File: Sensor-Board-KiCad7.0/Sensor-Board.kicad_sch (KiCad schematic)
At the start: 78 parts, among them J1 110990030, J11 9401-0-15-15-23-27-10-0, J2 9401-0-15-15-23-27-10-0, J3 9401-0-15-15-23-27-10-0, J4 9401-0-15-15-23-27-10-0, J5 9401-0-15-15-23-27-10-0, J6 9401-0-15-15-23-27-10-0, J7 9401-0-15-15-23-27-10-0, J8 9401-0-15-15-23-27-10-0, J9 9401-0-15-15-23-27-10-0, U1 LMV721, U10 BME680, U11 NAU7802_24-bit_ADC, U12 NAU7802_24-bit_ADC, U13 TCA9548AMRGER, U2 LMV721, U20 MMBFJ177LT1G, U27 MMBFJ177LT1G, U28 MMBFJ177LT1G, U3 LMV721, U4 LMV721, U5 LMV721, U6 OPAMP, U7 PS1-NO2-50, U8 PS1-CO-1000, U9 PS1-SO2-50

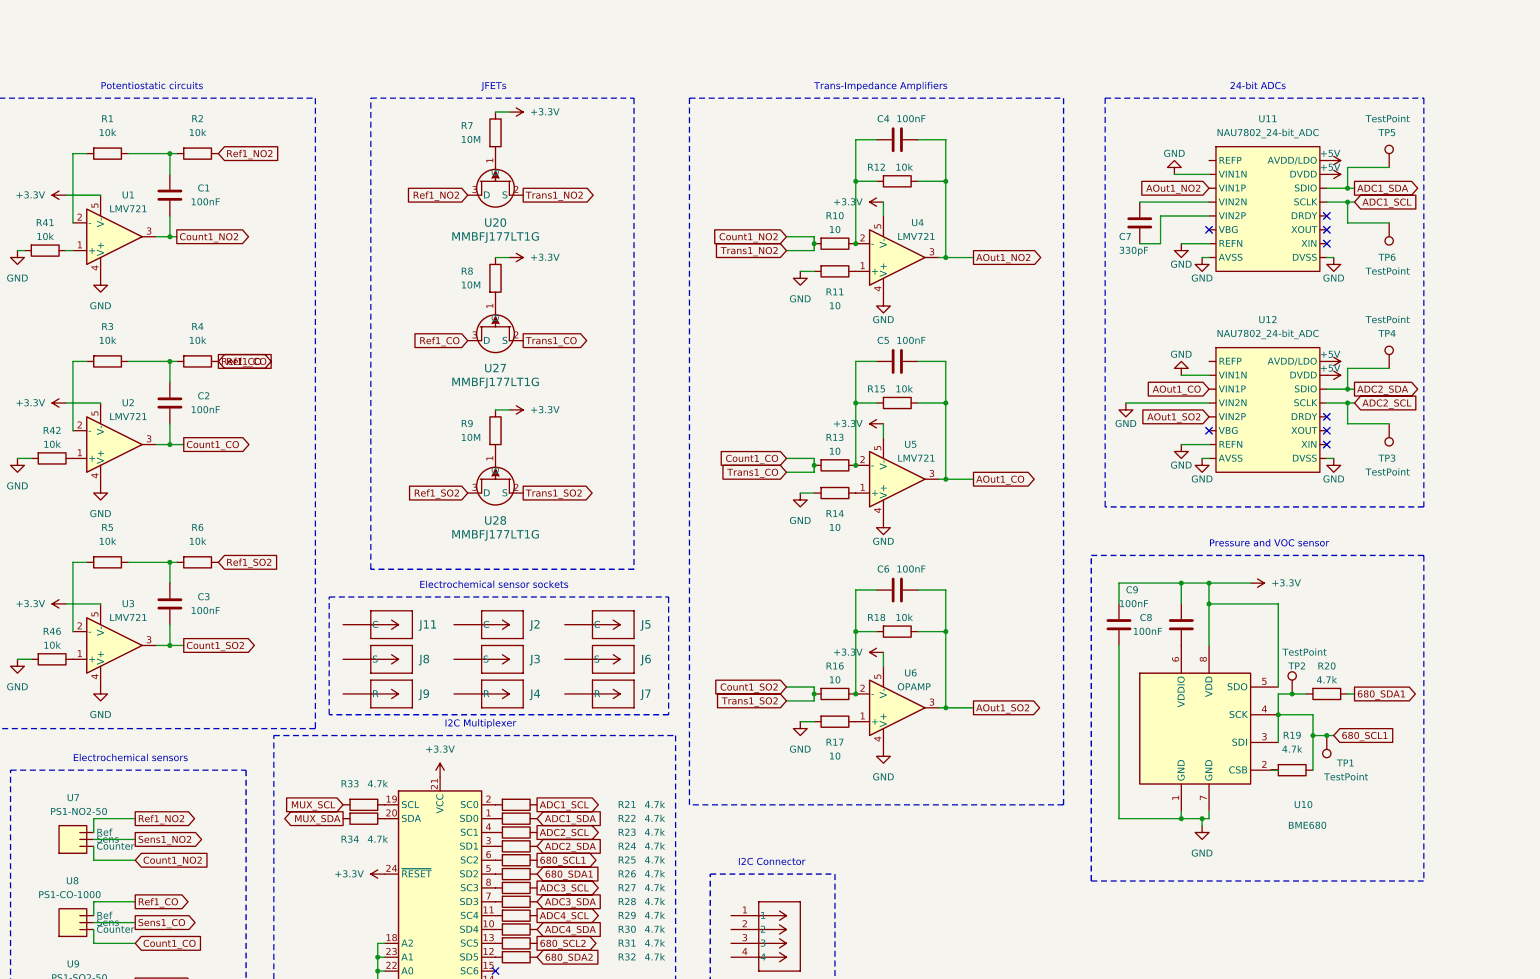
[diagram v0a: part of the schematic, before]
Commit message: Final check
Added 10k resistors to + input of opamps. Added JFET symbol and footprint. Changed opamp from LMV721 to OPA386 to conform to 3-electrode design sheet. Fixed circuit for BME680. Added test points.
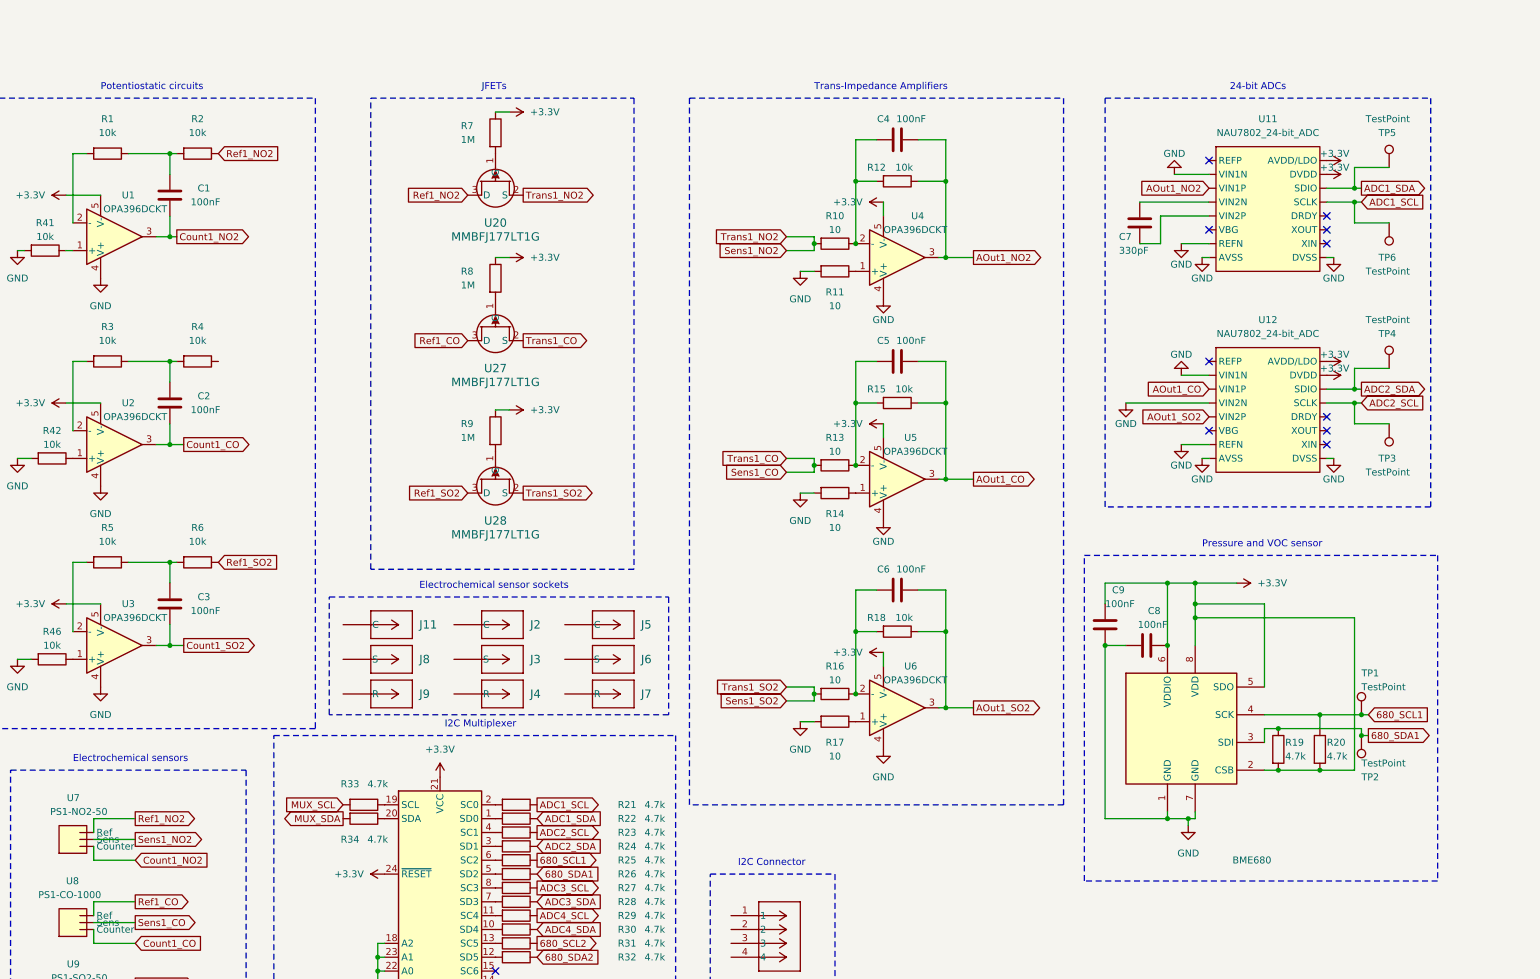
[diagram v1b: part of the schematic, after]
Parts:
- R7, R8, R9: value 10M -> 1M
- U1, U2, U3, U4, U5: value LMV721 -> OPA396DCKT
- U6: value OPAMP -> OPA396DCKT
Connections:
- net +5V is gone; now on net GND: U11. (XOUT), U12. (XOUT)
- net +3.3V: now also C8.2, R19.2, R20.2, U10.2 (CSB), U10.6 (VDDIO), U11. (XOUT), U12. (XOUT); no longer C8.1
- net 680_SCL1: now also R20.1; no longer R19.1, R20.2, TP2.1, U10.3 (SDI)
- net 680_SDA1: now also R19.1, TP2.1, U10.3 (SDI); no longer R20.1
- net Count1_CO: no longer R13.2, U27.2 (S)
- net Count1_NO2: no longer R10.2, U20.2 (S)
- net Count1_SO2: no longer R16.2, U28.2 (S)
- net GND: now also C8.1
- net Ref1_CO: no longer R4.1
- net Sens1_CO: now also R13.2, U27.2 (S)
- net Sens1_NO2: now also R10.2, U20.2 (S)
- net Sens1_SO2: now also R16.2, U28.2 (S)
- no-connect marks 12 -> 14
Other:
- moved on the sheet: C8, C9

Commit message: Updated symbols + footprints
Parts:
- removed C5, C6: 100nF, symbol Device:C
- removed C7: 330pF, symbol Device:C
- removed R10, R11, R13, R14, R16, R17: 10, symbol Device:R
- removed R12, R15, R18: 10k, symbol Device:R
- removed TP3, TP4, TP5, TP6: TestPoint, symbol Connector:TestPoint
- removed U1, U2, U3, U4, U5, U6: OPA396DCKT, symbol pspice:OPAMP
- removed U11, U12: NAU7802_24-bit_ADC, symbol ADCs:NAU7802_24-bit_ADC
- removed U20, U27, U28: MMBFJ177LT1G, SOT_77LT1G_ONS, symbol MMBFJ177LT1-D:MMBFJ177LT1G
- removed U7: PS1-NO2-50, symbol ElectrochemcialSensors:PS1-NO2-50
- removed U8: PS1-CO-1000, symbol ElectrochemcialSensors:PS1-CO-1000
- removed U9: PS1-SO2-50, symbol ElectrochemcialSensors:PS1-SO2-50
- added C19, C20, C21: 100nF, symbol Device:C
- added R52, R53, R67, R68: 10, symbol Device:R
- added R54, R56, R57, R69: 10k, symbol Device:R
- added R55: 100k, symbol Device:R
- added TP11, TP12, TP13, TP14, TP15, TP16, TP17, TP18: TestPoint, symbol Connector:TestPoint
- added U1, U2, U27, U28, U3, U34: OPA396DCKT, SC_96DCKT_TEX, symbol OPA396DCKT:OPA396DCKT
- added U20, U32, U33: MMBFJ177LT1, SOT-23-3_1P4X3P040_ONS, symbol MMBFJ177LT1G:MMBFJ177LT1
- added U4, U5: NAU7802SGI, SOI16_NAU7802SGI_NUV, symbol NAU7802:NAU7802SGI
- C4: value 100nF -> 330pF
- R1, R4: value 10k -> 100k
- R41, R42, R46: value 10k -> 1M
- R7, R8: value 1M -> 10
- R9: value 1M -> 10k
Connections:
- net 680_SDA1 is gone; now on net 680_SCL1: R19.1, R26.1, TP2.1, U10.3 (SDI)
- net +3.3V: now also J1.4, R41.2, R42.2, R46.2, U1.2 (V-), U2.2 (V-), U27.2 (V-), U28.2 (V-), U3.2 (V-), U34.2 (V-), U4.15 (DVDD), U5.15 (DVDD); no longer R7.1, R8.1, R9.1
- net ADC1_SCL: now also TP15.1, U4.13 (SCLK)
- net ADC1_SDA: now also TP14.1, U4.14 (SDIO)
- net ADC2_SCL: now also TP18.1, U5.13 (SCLK)
- net ADC2_SDA: now also TP17.1, U5.14 (SDIO)
- net AOut1_CO: now also C19.1, R54.1, U28.4 (OUT), U5.3 (VIN1P)
- net AOut1_NO2: now also C3.1, R9.1, U27.4 (OUT), U4.3 (VIN1P); no longer C4.1
- net AOut1_SO2: now also C21.1, R69.1, U34.4 (OUT), U5.5 (VIN2P)
- net Count1_CO: now also C1.2, J2. (C), U2.4 (OUT); no longer C2.2
- net Count1_NO2: now also J11. (C), C20.2, U1.4 (OUT); no longer C1.2
- net Count1_SO2: now also C2.2, J5. (C), U3.4 (OUT); no longer C3.2
- net GND: now also J1.1, R1.2, R4.2, R7.2, R53.2, R55.2, R68.2, U1.5 (V+), U2.5 (V+), U27.5 (V+), U28.5 (V+), U3.5 (V+), U34.5 (V+), U4.2 (VIN1N), U4.7 (REFN), U4.8 (AVSS), U4.9 (DVSS), U5.2 (VIN1N), U5.4 (VIN2N), U5.7 (REFN), U5.8 (AVSS), U5.9 (DVSS); no longer R41.2, R42.2, R46.2
- net MUX_SCL: now also J1.3, TP11.1
- net MUX_SDA: now also J1.2, TP12.1
- net Ref1_CO: now also J4. (R), R3.1, U32.1 (D)
- net Ref1_NO2: now also J9. (R), R57.1, U20.1 (D); no longer R2.1
- net Ref1_SO2: now also J7. (R), U33.1 (D)
- net Sens1_CO: now also J3. (S), R52.2, U32.2 (S)
- net Sens1_NO2: now also J8. (S), R8.2, U20.2 (S)
- net Sens1_SO2: now also J6. (S), R67.2, U33.2 (S)
- net at R9.2: now also C3.2, R8.1, U27.3 (-IN)
- net at R42.1: now also U32.3 (G)
- net at R3.2: now also C1.1, R2.1
- net at R46.1: now also U33.3 (G)
- net at R5.2: now also U3.3 (-IN)
- net at R5.1, R6.2: now also C2.1; no longer C3.1
- net at R41.1: now also U20.3 (G)
- net at C4.2: now also U4.5 (VIN2P)
- net at R4.1: now also U3.1 (+IN)
- new net: C19.2, R52.1, R54.2, U28.3 (-IN)
- new net: TP16.1, U5.16 (AVDD/LDO)
- new net: C4.1, U4.4 (VIN2N)
- new net: R7.1, U27.1 (+IN)
- new net: R53.1, U28.1 (+IN)
- new net: TP13.1, U4.16 (AVDD/LDO)
- new net: R2.2, U2.3 (-IN)
- new net: C20.1, R56.1, R57.2
- new net: C21.2, R67.1, R69.2, U34.3 (-IN)
- new net: R68.1, U34.1 (+IN)
- new net: R1.1, U2.1 (+IN)
- new net: R56.2, U1.3 (-IN)
- new net: R55.1, U1.1 (+IN)
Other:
- note removed: "Electrochemical sensors"
- moved on the sheet: C8, C9, J1, J11, J8, J9, R19, R20, R21, R22, R23, R24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

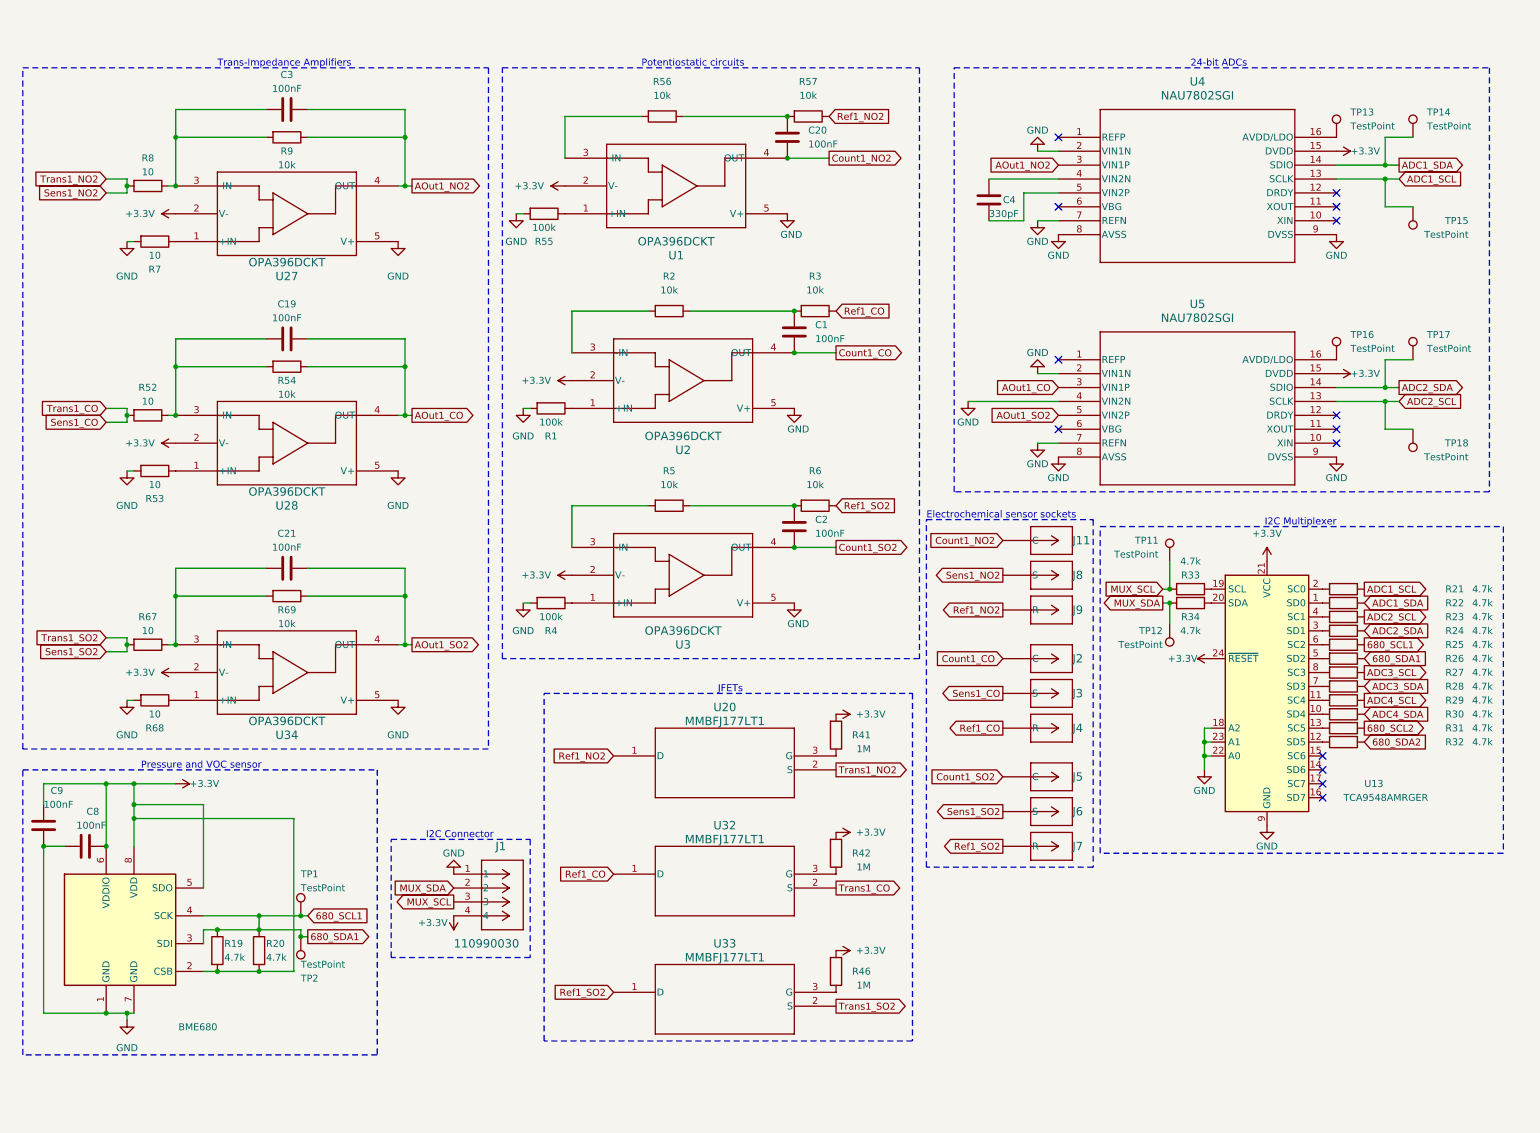
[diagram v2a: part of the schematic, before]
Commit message: Fixed a bunch of errors
Updated OPA396 symbol + footprints
Updated NAU7802 symbol + footprints
Updated MMBFJ177LT1 symbol + footprints
Updated EChem socket symbol + footprints
Updated I2C connector symbol + footprints
Fixed connection issues with EChem sockets
Removed net labels from EChem sockets
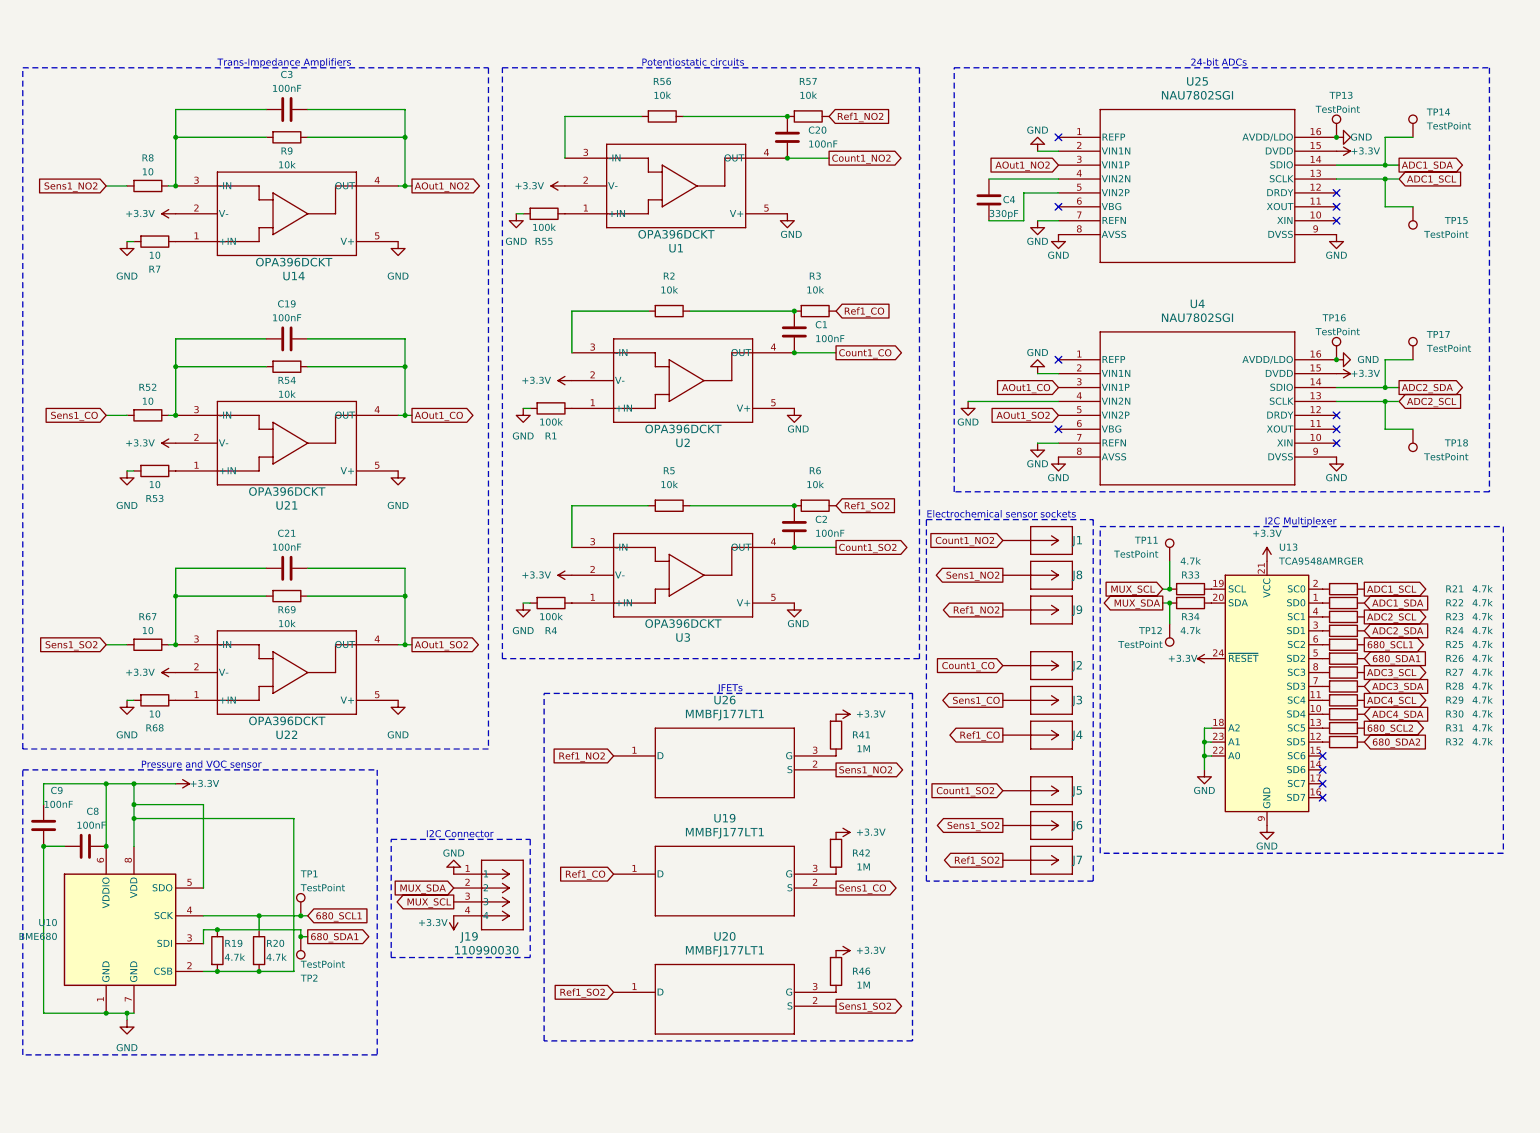
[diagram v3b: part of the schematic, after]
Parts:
- removed J1: 110990030, CONN_110990030_SEE, symbol 110990030:110990030
- removed J11, J2, J3, J4, J5, J6, J7, J8, J9: 9401-0-15-15-23-27-10-0, CONN_0384-0-67-80-23-27-10-0_MIM, symbol EChem Socket:9401-0-15-15-23-27-10-0
- removed U27, U28, U34: OPA396DCKT, SC_96DCKT_TEX, symbol OPA396DCKT:OPA396DCKT
- removed U32, U33: MMBFJ177LT1, SOT-23-3_1P4X3P040_ONS, symbol MMBFJ177LT1G:MMBFJ177LT1
- removed U5: NAU7802SGI, SOI16_NAU7802SGI_NUV, symbol NAU7802:NAU7802SGI
- added J1, J2, J3, J4, J5, J6, J7, J8, J9: 9401-0-15-15-23-27-10-0, CONN_0384-0-67-80-23-27-10-0_MIM, symbol EChem socket:9401-0-15-15-23-27-10-0
- added J19: 110990030, CONN_110990030_SEE, symbol I2C Connector:110990030
- added U14, U21, U22: OPA396DCKT, SC_96DCKT_TEX, symbol OPA396DCKT:OPA396DCKT
- added U19, U26: MMBFJ177LT1, SOT-23-3_1P4X3P040_ONS, symbol MMBFJ177LT1G:MMBFJ177LT1
- added U25: NAU7802SGI, SOI16_NAU7802SGI_NUV, symbol NAU7802:NAU7802SGI
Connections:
- net +3.3V: now also J19.4, U14.2 (V-), U21.2 (V-), U22.2 (V-), U25.15 (DVDD)
- net 680_SCL1: no longer R19.1, R26.1, TP2.1, U10.3 (SDI)
- net ADC1_SCL: now also U25.13 (SCLK); no longer U4.13 (SCLK)
- net ADC1_SDA: now also U25.14 (SDIO); no longer U4.14 (SDIO)
- net ADC2_SCL: now also U4.13 (SCLK)
- net ADC2_SDA: now also U4.14 (SDIO)
- net AOut1_CO: now also U4.3 (VIN1P), U21.4 (OUT)
- net AOut1_NO2: now also U14.4 (OUT), U25.3 (VIN1P); no longer U4.3 (VIN1P)
- net AOut1_SO2: now also U4.5 (VIN2P), U22.4 (OUT)
- net Count1_CO: now also J2.
- net Count1_NO2: now also J1.
- net Count1_SO2: now also J5.
- net GND: now also TP13.1, TP16.1, U4.16 (AVDD/LDO), U4.4 (VIN2N), J19.1, U14.5 (V+), U21.5 (V+), U22.5 (V+), U25.16 (AVDD/LDO), U25.2 (VIN1N), U25.7 (REFN), U25.8 (AVSS), U25.9 (DVSS)
- net MUX_SCL: now also J19.3
- net MUX_SDA: now also J19.2
- net Ref1_CO: now also J4., U19.1 (D)
- net Ref1_NO2: now also J9., U26.1 (D); no longer U20.1 (D)
- net Ref1_SO2: now also U20.1 (D), J7.
- net Sens1_CO: now also J3., U19.2 (S)
- net Sens1_NO2: now also J8., U26.2 (S); no longer U20.2 (S)
- net Sens1_SO2: now also U20.2 (S), J6.
- net at C19.2, R52.1, R54.2: now also U21.3 (-IN)
- net at C4.1: now also U25.4 (VIN2N); no longer U4.4 (VIN2N)
- net at C4.2: now also U25.5 (VIN2P); no longer U4.5 (VIN2P)
- net at R7.1: now also U14.1 (+IN)
- net at R53.1: now also U21.1 (+IN)
- net at R41.1: now also U26.3 (G); no longer U20.3 (G)
- net at R46.1: now also U20.3 (G)
- net at C21.2, R67.1, R69.2: now also U22.3 (-IN)
- net at R42.1: now also U19.3 (G)
- net at R68.1: now also U22.1 (+IN)
- net at C3.2, R8.1, R9.2: now also U14.3 (-IN)
- new net 680_SDA1: R19.1, R26.1, TP2.1, U10.3 (SDI)
